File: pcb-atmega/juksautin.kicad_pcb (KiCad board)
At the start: 2 copper layers, 65 x 35 mm, 31 parts, among them J1 Screw_Terminal_01x09, J2 Power out, J3 USB_C_Receptacle_USB2.0, J4 TagConnect, J5 EXTRA, J6 AREF_OUT, U1 SP3485EN, U2 SRV05-4, U3 LM2576S-5, U4 ATmega32U4-AU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

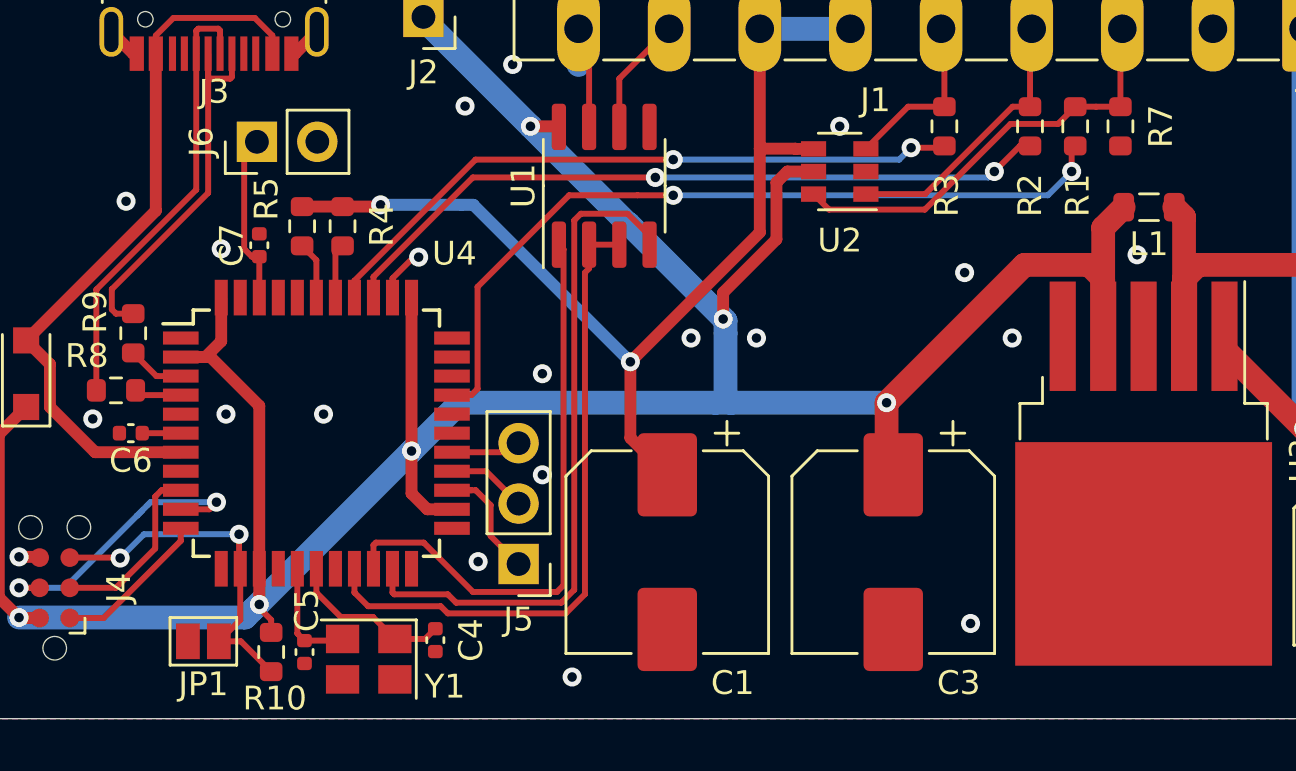
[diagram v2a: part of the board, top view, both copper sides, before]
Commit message: pcb: Make schema a bit more readable
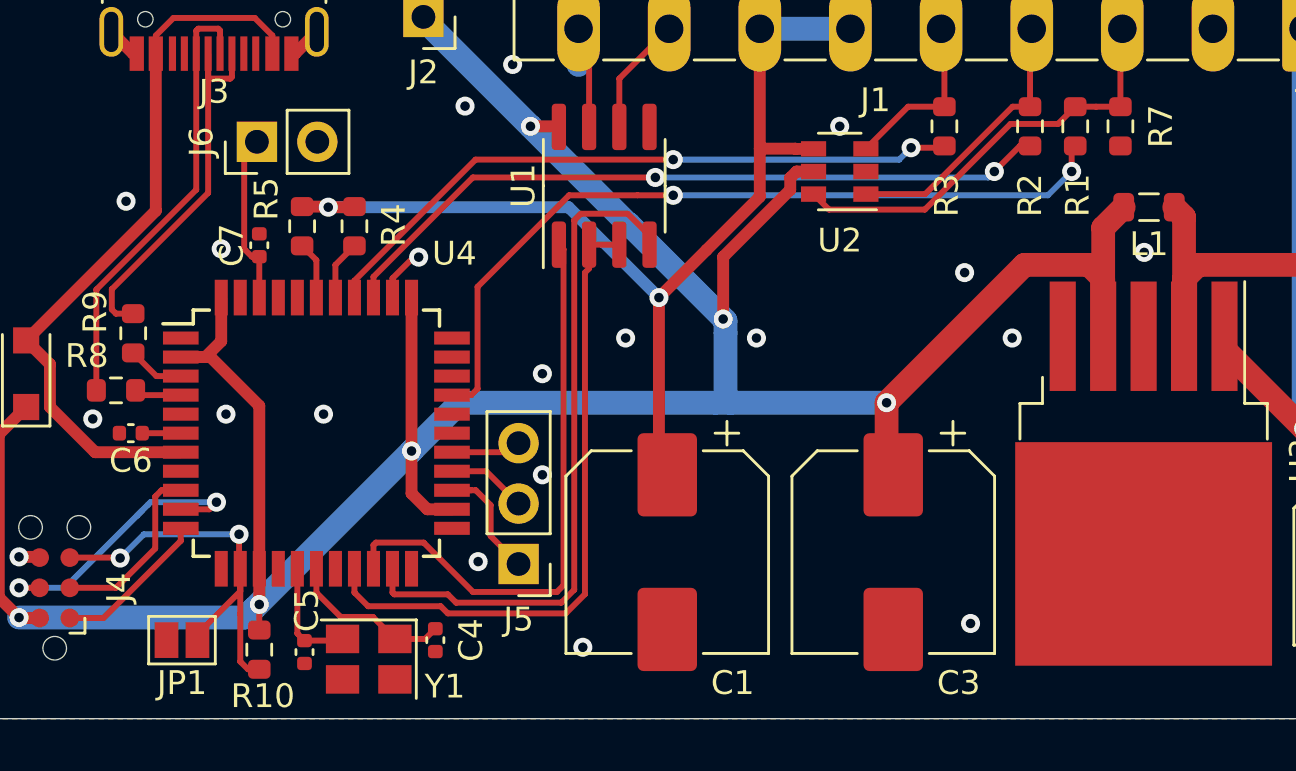
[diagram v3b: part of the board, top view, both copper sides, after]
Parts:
- moved JP1 0.90 mm to (119.3, 96.7)
- moved R10 0.51 mm to (122.6, 97.1)
- moved R4 0.50 mm to (126.6, 79.3)
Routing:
- net /RESET: track 15.2 -> 17.6 mm
- net VCC: track 133.2 -> 132.6 mm
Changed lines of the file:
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@@
     (thickness 1.6)
     (drawings 30)
-    (tracks 293)
+    (tracks 297)
     (zones 0)
     (modules 31)
@@
   )
   (setup
-    (last_trace_width 0.25)
+    (last_trace_width 0.5)
     (user_trace_width 0.25)
     (user_trace_width 0.5)
@@
   )
   (module Resistor_SMD:R_0603_1608Metric (layer F.Cu)
-    (at 123.1 97.2 270)
+    (at 122.6 97.1 270)
     (descr "Resistor SMD 0603 (1608 Metric), square (rectangular) end terminal, IPC_7351 nominal, (Body size source: IPC-SM-782 page 72, https://www.pcb-3d.com/wordpress/wp-content/uploads/ipc-sm-782a_amendment_1_and_2.pdf), generated with kicad-footprint-generator")
     (tags resistor)
@@
   )
   (module Resistor_SMD:R_0603_1608Metric (layer F.Cu)
-    (at 126.1 79.3 90)
+    (at 126.6 79.3 90)
     (descr "Resistor SMD 0603 (1608 Metric), square (rectangular) end terminal, IPC_7351 nominal, (Body size source: IPC-SM-782 page 72, https://www.pcb-3d.com/wordpress/wp-content/uploads/ipc-sm-782a_amendment_1_and_2.pdf), generated with kicad-footprint-generator")
     (tags resistor)
@@
   )
   (module Jumper:SolderJumper-2_P1.3mm_Open_Pad1.0x1.5mm (layer F.Cu)
-    (at 120.25 96.75 180)
+    (at 119.35 96.7 180)
     (descr "SMD Solder Jumper, 1x1.5mm Pads, 0.3mm gap, open")
     (tags "solder jumper open")
@@
   (via (at 129.3 80.6) (size 0.8) (drill 0.4) (layers F.Cu B.Cu) (net 2))
   (via (at 154.25 84) (size 0.8) (drill 0.4) (layers F.Cu B.Cu) (net 2))
-  (via (at 159.5 80.5) (size 0.8) (drill 0.4) (layers F.Cu B.Cu) (net 2))
+  (via (at 159.8 80.4) (size 0.8) (drill 0.4) (layers F.Cu B.Cu) (net 2))
   (via (at 152.25 81.25) (size 0.8) (drill 0.4) (layers F.Cu B.Cu) (net 2))
   (via (at 112.5 93.2) (size 0.8) (drill 0.4) (layers F.Cu B.Cu) (net 2))
@@
   (via (at 134.5 89.75) (size 0.8) (drill 0.4) (layers F.Cu B.Cu) (net 2))
   (via (at 134.5 85.5) (size 0.8) (drill 0.4) (layers F.Cu B.Cu) (net 2))
-  (via (at 135.75 98.25) (size 0.8) (drill 0.4) (layers F.Cu B.Cu) (net 2))
-  (via (at 140.75 84) (size 0.8) (drill 0.4) (layers F.Cu B.Cu) (net 2))
+  (via (at 136.2 97) (size 0.8) (drill 0.4) (layers F.Cu B.Cu) (net 2))
+  (via (at 138 84) (size 0.8) (drill 0.4) (layers F.Cu B.Cu) (net 2))
   (via (at 143.5 84) (size 0.8) (drill 0.4) (layers F.Cu B.Cu) (net 2))
   (via (at 121 80.25) (size 0.8) (drill 0.4) (layers F.Cu B.Cu) (net 2))
@@
   (segment (start 122.6 95.15) (end 122.6 93.7) (width 0.5) (layer F.Cu) (net 3))
   (via (at 122.6 95.2) (size 0.8) (drill 0.4) (layers F.Cu B.Cu) (net 3))
-  (segment (start 123.1 96.575) (end 123.1 95.85) (width 0.25) (layer F.Cu) (net 3))
-  (segment (start 123.1 95.85) (end 122.5 95.25) (width 0.25) (layer F.Cu) (net 3))
   (segment (start 122.5 95.25) (end 122.6 95.15) (width 0.5) (layer F.Cu) (net 3))
-  (segment (start 144.34001 79.849952) (end 142.1 82.089962) (width 0.5) (layer F.Cu) (net 3))
-  (segment (start 144.34001 77.45999) (end 144.34001 79.849952) (width 0.5) (layer F.Cu) (net 3))
-  (segment (start 142.1 82.089962) (end 142.1 83.2) (width 0.5) (layer F.Cu) (net 3))
-  (segment (start 144.8 77) (end 144.34001 77.45999) (width 0.5) (layer F.Cu) (net 3))
-  (segment (start 145.9 77) (end 144.8 77) (width 0.5) (layer F.Cu) (net 3))
+  (segment (start 122.6 96.175) (end 122.8 96.375) (width 0.25) (layer F.Cu) (net 3))
+  (segment (start 122.6 95.2) (end 122.6 96.175) (width 0.25) (layer F.Cu) (net 3))
+  (segment (start 142.1 83.2) (end 142.1 80.589962) (width 0.5) (layer F.Cu) (net 3))
+  (segment (start 145.184998 77) (end 145.9 77) (width 0.5) (layer F.Cu) (net 3))
+  (segment (start 144.919999 77.264999) (end 145.184998 77) (width 0.5) (layer F.Cu) (net 3))
+  (segment (start 144.919999 77.769963) (end 144.919999 77.264999) (width 0.5) (layer F.Cu) (net 3))
+  (segment (start 142.1 80.589962) (end 144.919999 77.769963) (width 0.5) (layer F.Cu) (net 3))
   (segment (start 136.02 71) (end 136.02 72.52) (width 1) (layer B.Cu) (net 4) (status 30))
   (segment (start 136.465 71.445) (end 136.02 71) (width 0.25) (layer F.Cu) (net 4))
@@
   (segment (start 121.75 93.65) (end 121.8 93.7) (width 0.25) (layer F.Cu) (net 16))
   (segment (start 121.75 92.25) (end 121.75 93.65) (width 0.25) (layer F.Cu) (net 16))
-  (segment (start 121.8 95.85) (end 120.9 96.75) (width 0.25) (layer F.Cu) (net 16))
-  (segment (start 121.8 93.7) (end 121.8 95.85) (width 0.25) (layer F.Cu) (net 16))
-  (segment (start 121.825 96.75) (end 123.1 98.025) (width 0.25) (layer F.Cu) (net 16))
-  (segment (start 120.9 96.75) (end 121.825 96.75) (width 0.25) (layer F.Cu) (net 16))
   (segment (start 117.75 92.25) (end 116.75 93.25) (width 0.25) (layer B.Cu) (net 16))
   (segment (start 121.75 92.25) (end 117.75 92.25) (width 0.25) (layer B.Cu) (net 16))
+  (segment (start 122.125 97.925) (end 121.8 97.6) (width 0.25) (layer F.Cu) (net 16))
+  (segment (start 122.6 97.925) (end 122.125 97.925) (width 0.25) (layer F.Cu) (net 16))
+  (segment (start 121.8 97.6) (end 121.8 95.6) (width 0.25) (layer F.Cu) (net 16))
+  (segment (start 121.8 93.7) (end 121.8 95.6) (width 0.25) (layer F.Cu) (net 16))
+  (segment (start 121.8 94.65) (end 121.8 93.7) (width 0.25) (layer F.Cu) (net 16))
+  (segment (start 120 96.45) (end 121.8 94.65) (width 0.25) (layer F.Cu) (net 16))
+  (segment (start 120 96.7) (end 120 96.45) (width 0.25) (layer F.Cu) (net 16))
   (via (at 112.5 94.5) (size 0.8) (drill 0.4) (layers F.Cu B.Cu) (net 17))
   (segment (start 112.5 94.5) (end 114.426998 94.5) (width 0.25) (layer B.Cu) (net 17))
@@
   (segment (start 149.5 76.5) (end 150 76) (width 0.25) (layer B.Cu) (net 25))
   (segment (start 140 76.5) (end 149.5 76.5) (width 0.25) (layer B.Cu) (net 25))
-  (segment (start 125.8 80.425) (end 126.1 80.125) (width 0.25) (layer F.Cu) (net 26))
-  (segment (start 125.8 82.3) (end 125.8 80.425) (width 0.25) (layer F.Cu) (net 26))
+  (segment (start 125.8 80.925) (end 126.6 80.125) (width 0.25) (layer F.Cu) (net 26))
+  (segment (start 125.8 82.3) (end 125.8 80.925) (width 0.25) (layer F.Cu) (net 26))
   (segment (start 125 80.725) (end 124.4 80.125) (width 0.25) (layer F.Cu) (net 27))
   (segment (start 125 82.3) (end 125 80.725) (width 0.25) (layer F.Cu) (net 27))
@@
   (segment (start 131.585003 94.675001) (end 129.510003 92.600001) (width 0.25) (layer F.Cu) (net 30))
   (segment (start 135.110001 94.675001) (end 131.585003 94.675001) (width 0.25) (layer F.Cu) (net 30))
-  (segment (start 124.4 78.475) (end 126.1 78.475) (width 0.5) (layer F.Cu) (net 31))
   (segment (start 143.64 71) (end 147.45 71) (width 1) (layer B.Cu) (net 31))
   (segment (start 143.6 71.04) (end 143.64 71) (width 0.5) (layer F.Cu) (net 31))
-  (segment (start 131.6 78.4) (end 131.1 78.4) (width 0.5) (layer B.Cu) (net 31))
-  (segment (start 138.2 85) (end 131.6 78.4) (width 0.5) (layer B.Cu) (net 31))
-  (segment (start 126.1 78.475) (end 127.625 78.475) (width 0.5) (layer F.Cu) (net 31))
-  (segment (start 127.7 78.4) (end 131.1 78.4) (width 0.5) (layer B.Cu) (net 31))
-  (segment (start 127.625 78.475) (end 127.7 78.4) (width 0.5) (layer F.Cu) (net 31))
-  (via (at 138.2 85) (size 0.8) (drill 0.4) (layers F.Cu B.Cu) (net 31))
-  (via (at 127.7 78.4) (size 0.8) (drill 0.4) (layers F.Cu B.Cu) (net 31))
-  (segment (start 138.2 88.2) (end 139.75 89.75) (width 0.5) (layer F.Cu) (net 31))
-  (segment (start 138.2 85) (end 138.2 88.2) (width 0.5) (layer F.Cu) (net 31))
-  (segment (start 138.2 85) (end 143.64 79.56) (width 0.5) (layer F.Cu) (net 31))
+  (via (at 139.4 82.3) (size 0.8) (drill 0.4) (layers F.Cu B.Cu) (net 31))
   (segment (start 145.135035 76.04) (end 143.64 76.04) (width 0.5) (layer F.Cu) (net 31))
   (segment (start 145.145035 76.05) (end 145.135035 76.04) (width 0.5) (layer F.Cu) (net 31))
   (segment (start 145.9 76.05) (end 145.145035 76.05) (width 0.5) (layer F.Cu) (net 31))
   (segment (start 143.64 76.04) (end 143.64 71) (width 0.5) (layer F.Cu) (net 31))
-  (segment (start 143.64 79.56) (end 143.64 76.04) (width 0.5) (layer F.Cu) (net 31))
+  (via (at 125.5 78.5) (size 0.8) (drill 0.4) (layers F.Cu B.Cu) (net 31))
+  (segment (start 143.64 76.04) (end 143.64 78.06) (width 0.5) (layer F.Cu) (net 31))
+  (segment (start 125.475 78.475) (end 125.5 78.5) (width 0.5) (layer F.Cu) (net 31))
+  (segment (start 124.4 78.475) (end 125.475 78.475) (width 0.5) (layer F.Cu) (net 31))
+  (segment (start 126.575 78.5) (end 126.6 78.475) (width 0.5) (layer F.Cu) (net 31))
+  (segment (start 125.5 78.5) (end 126.575 78.5) (width 0.5) (layer F.Cu) (net 31))
+  (segment (start 135.6 78.5) (end 139.4 82.3) (width 0.5) (layer B.Cu) (net 31))
+  (segment (start 125.5 78.5) (end 135.6 78.5) (width 0.5) (layer B.Cu) (net 31))
+  (segment (start 141.399992 80.300008) (end 139.4 82.3) (width 0.5) (layer F.Cu) (net 31))
+  (segment (start 143.64 78.06) (end 141.399992 80.300008) (width 0.5) (layer F.Cu) (net 31))
+  (segment (start 139.4 89.4) (end 139.75 89.75) (width 0.5) (layer F.Cu) (net 31))
+  (segment (start 139.4 82.3) (end 139.4 89.4) (width 0.5) (layer F.Cu) (net 31))
   (segment (start 133.12 88.8) (end 133.5 88.42) (width 0.25) (layer F.Cu) (net 32))
   (segment (start 130.7 88.8) (end 133.12 88.8) (width 0.25) (layer F.Cu) (net 32))

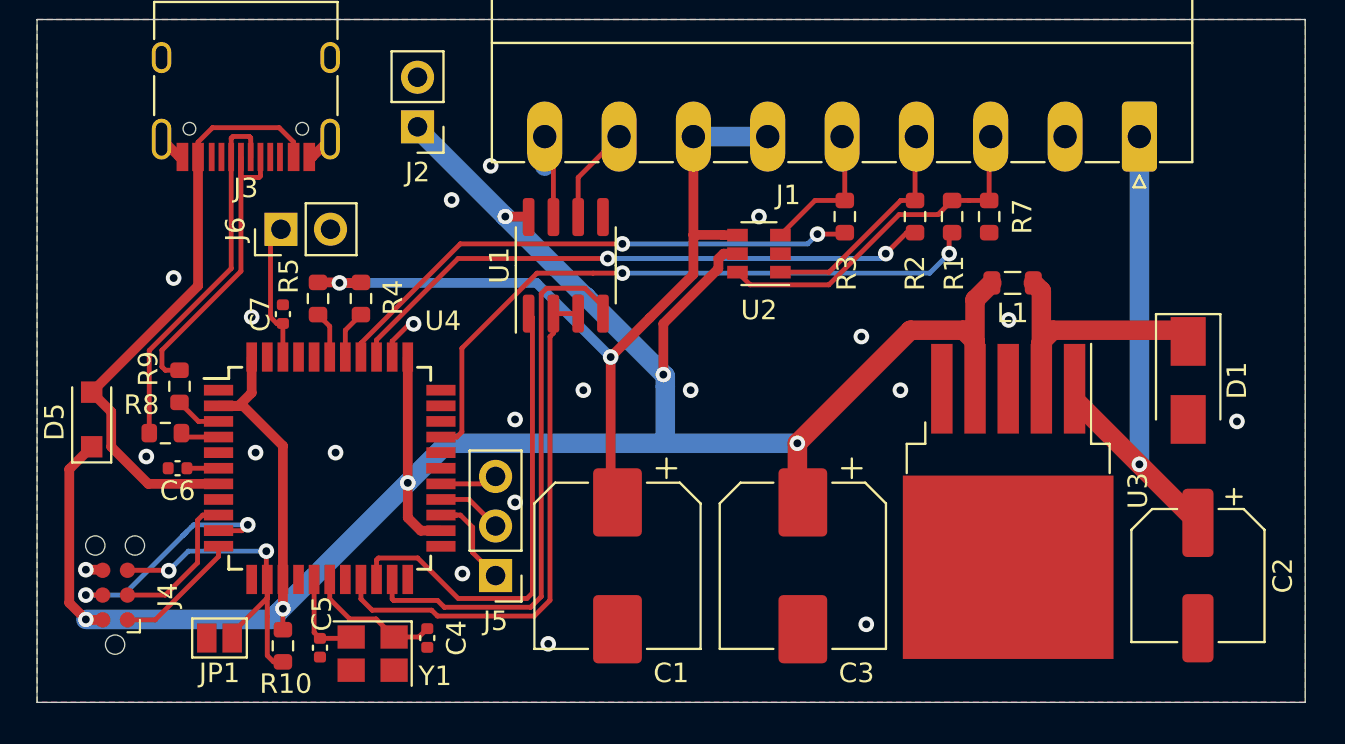
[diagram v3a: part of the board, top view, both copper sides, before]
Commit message: pcb: Replace LM2576 with Recom R-78E5.0 THT DC/DC converter
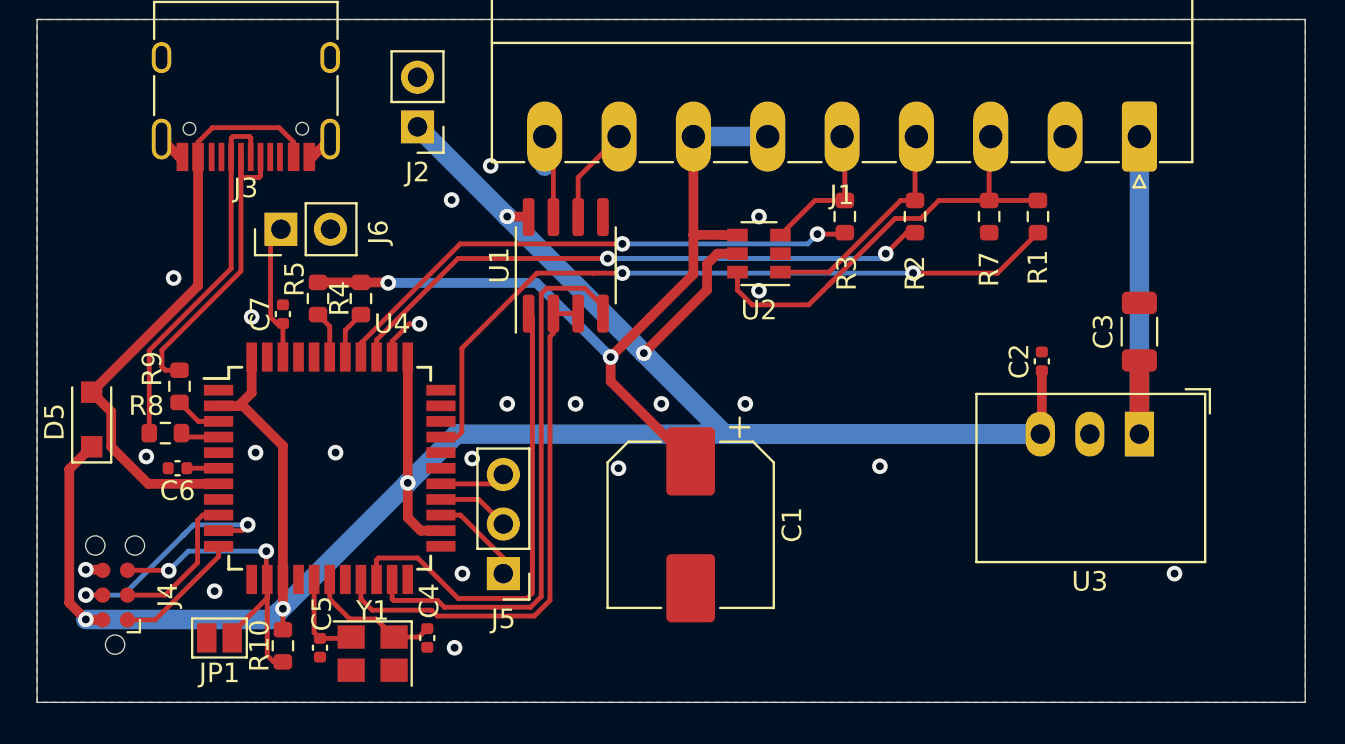
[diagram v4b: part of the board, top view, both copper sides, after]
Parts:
- removed D1: SS34, Diode_SMD:D_SMA
- removed L1: 100uH, Inductor_SMD:L_0805_2012Metric
- C2: value 100u -> 10u; footprint Capacitor_SMD:CP_Elec_6.3x7.7 -> Capacitor_SMD:C_0402_1005Metric
- C3: value 1000u -> 10u; footprint Capacitor_SMD:CP_Elec_8x10 -> Capacitor_SMD:C_1206_3216Metric
- U3: value LM2576S-5 -> R-78E5.0-0.5; footprint Package_TO_SOT_SMD:TO-263-5_TabPin3 -> Converter_DCDC:Converter_DCDC_RECOM_R-78E-0.5_THT
- moved C3 21.0 mm to (166.5, 81.0), turned to 90 degrees
- moved C2 13.6 mm to (161.5, 82.5), turned to 90 degrees
- moved U3 7.56 mm to (166.5, 86.2), turned to 180 degrees
- moved R1 4.40 mm to (161.3, 75.1)
- moved C1 4.30 mm to (143.5, 90.9)
- moved J5 0.41 mm to (133.9, 93.4)
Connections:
- C2 pad 1: VIN -> VCC
- C3 pad 1: VCC -> VIN
- U3 pad 2: Net-(D1-Pad1) -> GND
- U3 pad 3: GND -> VCC
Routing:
- net Net-(D1-Pad1): track 16.0 -> 0.00 mm
- net VCC: track 132.6 -> 141.8 mm, vias 6 -> 5
- net VIN: track 26.3 -> 19.0 mm, vias 1 -> 0
- net PUMPFAIL: track 18.3 -> 22.5 mm
- net /PUMPFAIL_M: track 33.7 -> 37.6 mm
- net K9: track 44.5 -> 42.8 mm
- net Net-(J5-Pad1): track 5.66 -> 4.91 mm
- net GND: vias 21 -> 22
